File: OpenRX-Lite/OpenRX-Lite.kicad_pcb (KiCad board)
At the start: 6 copper layers, 10 x 11.5 mm, 47 parts, among them U1 ESP32-C3, U2 TLV75533PDQNR, U3 SX1281IMLTRT, X1 CJ17-400001010B20

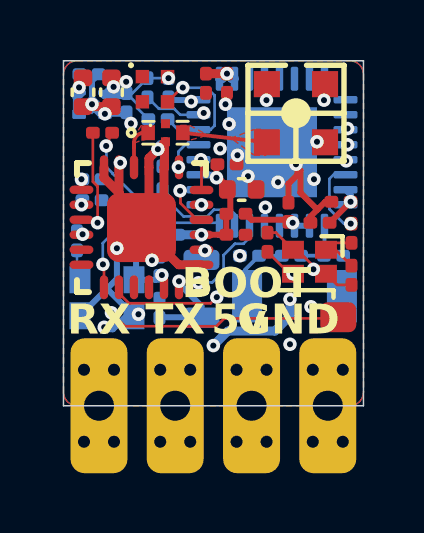
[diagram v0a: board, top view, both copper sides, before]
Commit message: Rev 2 board work: routing optimisations, logo placement, 3D model fixes
Routing reworked on Lite (segments 313 to 256, vias 60 to 89), Lite-UFL
(317 to 269, 61 to 85) and Gemini (682 to 688, 196 to 243). ExpressLRS logo
placed on Mono.

3D model fixes on Gemini and Mono:

- RFX2401C (U4, U7) pointed at QFN-16_L3.0-W3.0-H0.9-P0.50.wrl with an offset
  of (-951.61, 821.31, 0), so the body rendered about a metre off the board and
  the land looked bare in the viewer. Repointed at the RFX2401C model that
  OpenRX-Shared.pretty/QFN-16_L3.0-W3.0-P0.50-BL-EP1.7.kicad_mod specifies,
  offset zeroed, 270 degree rotation kept.
- SKY13373 (U5, U8) carried no model reference at all. Added, matching the
  library footprint.

The boards now agree with the shared library on both, so Update Footprints from
Library preserves this rather than reverting it.

DRC reviewed: zero unconnected items on all four boards. The remaining items
are pre-existing and understood. The shorting_items reports on Lite and
Lite-UFL are all netted-copper against unnetted copper inside the multi-hole
TP footprints, never signal to signal, and are present at the previous commit
too. The copper_edge_clearance reports are the TP1-TP4 castellated pads sitting
on the board edge by design.

Co-Authored-By: Claude Opus 5 (1M context) <noreply@anthropic.com>
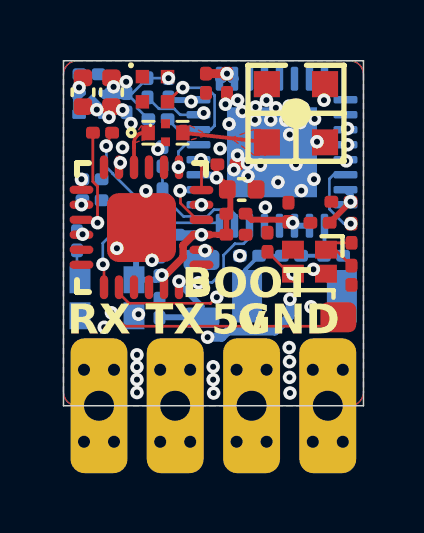
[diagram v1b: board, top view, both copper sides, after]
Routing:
- net GND: track 30.2 -> 1.51 mm, vias 25 -> 54
- net +3V3: track 22.4 -> 24.6 mm

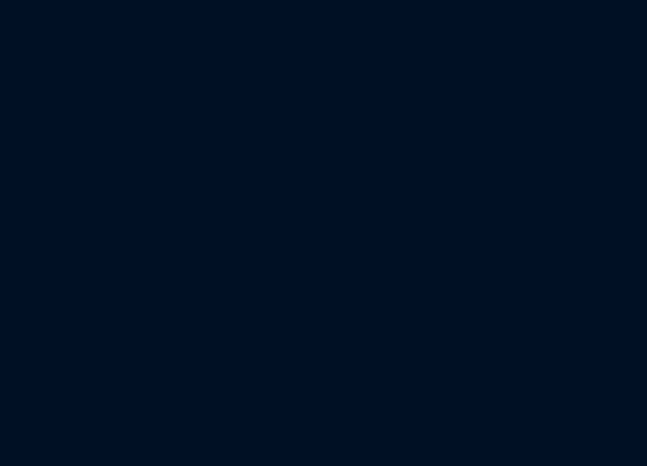
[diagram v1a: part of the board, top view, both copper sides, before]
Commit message: Rebuild E6 substitute STEP models from the trusted wrl geometry
The .step files beside these .wrl models were different parts (USB-C
3.5x oversized, etc), and the upstream LCSC .step is the same wrong
file, so kicad-cli --subst-models shipped wrong geometry in every STEP
export while the 3D viewer looked perfect. Rebuilt as tessellated STEP
solids from the .wrl the viewer renders, via
OpenDrone-Scripts/kicad/wrl_to_step.py: bbox and origin now match to
0.000 mm. check_models reports zero E6, export unblocked.

Co-Authored-By: Claude Opus 5 (1M context) <noreply@anthropic.com>
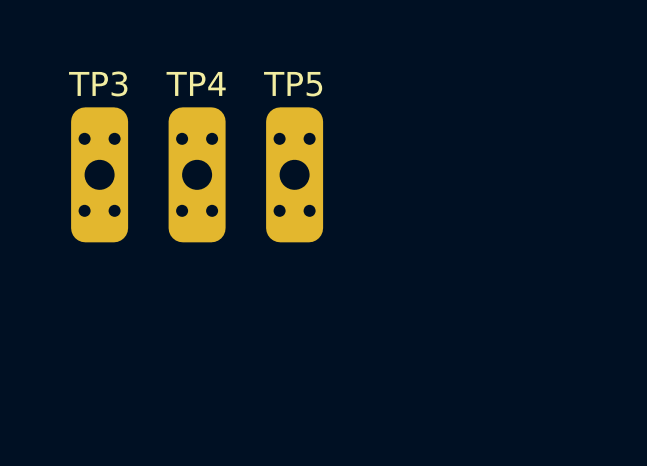
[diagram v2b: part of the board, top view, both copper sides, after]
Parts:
- added TP3: 5V, OpenRX-Shared:SolderPad_1.2x2.0mm, F.Cu at (1.12, 2.42)
- added TP4: GND, OpenRX-Shared:SolderPad_1.2x2.0mm, F.Cu at (4.38, 2.42)
- added TP5: BOOT, OpenRX-Shared:SolderPad_1.2x2.0mm, F.Cu at (7.62, 2.42)
